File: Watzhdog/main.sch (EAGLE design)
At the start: 44 parts, among them CN1 MICROUSB(MC-5F-02), IC1 C8051F381-GM, IC3 N25Q512A, IC6 MPU-9250, U1 MCP73831, U2 TPS61201

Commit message: 回路図修正完了 モジュールごとに見やすくした DCDC の高周波ラインを分離 各所パスコン追加 EEPROM のCS ラインにプルアップ追加
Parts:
- added C12, C14: 0.1u, reg,cap:C-1005
- added C13, C4: 22uF, CH_passive:CAP0805
- added R6: 100k, reg,cap:R-1005
- R26: value 1k -> 100k
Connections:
- net N$5 renamed PWR_EN_1
- net N$6 renamed PWR_EN
- net N$7 renamed PWR_EN_2
- removed net VBAT: C2.1, JP1.+, L1.2, R2.2, S1.1, S1.2, U1.VBAT, U2.VIN
- removed net VCC: C1.1, C10.P$2, C11.P$2, C6.1, C7.P$2, C9.P$2, IC1G$1.REGIN, IC1G$1.VDD, IC3G$1.!HOLD!/DQ3, IC3G$1.!WP!/VPP/DQ2, IC3G$1.VCC, IC6.RESV1, IC6.VDD, IC6.VDDIO, MP.TP, R11.P$2, U2.FB, U2.VOUT
- new net +3V3: C1.1, C10.P$2, C11.P$2, C13.1, C14.P$2, C6.1, C7.P$2, C9.P$2, IC1G$1.REGIN, IC1G$1.VDD, IC3G$1.!HOLD!/DQ3, IC3G$1.!WP!/VPP/DQ2, IC3G$1.VCC, IC6.RESV1, IC6.VDD, IC6.VDDIO, MP.TP, R11.P$2, R6.P$2, U2.FB, U2.VOUT
- new net PGND: C1.2, C12.P$1, C13.2, C4.2, U2.PAD@1, U2.PAD@2, U2.PAD@3, U2.PAD@4, U2.PAD@5, U2.PGND
- new net VDD_BATT: C12.P$2, C2.1, C4.1, JP1.+, L1.2, R2.2, S1.1, S1.2, U1.VBAT, U2.VIN
- net DGND: now also C14.P$1; no longer C1.2, U2.PAD@1, U2.PAD@2, U2.PAD@3, U2.PAD@4, U2.PAD@5, U2.PGND
- net EEPROM_!CS: now also R6.P$1
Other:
- moved on the sheet: C1, C10, C2, C3, C5, C6, CN1, D11, D2, D3, D4, FET1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

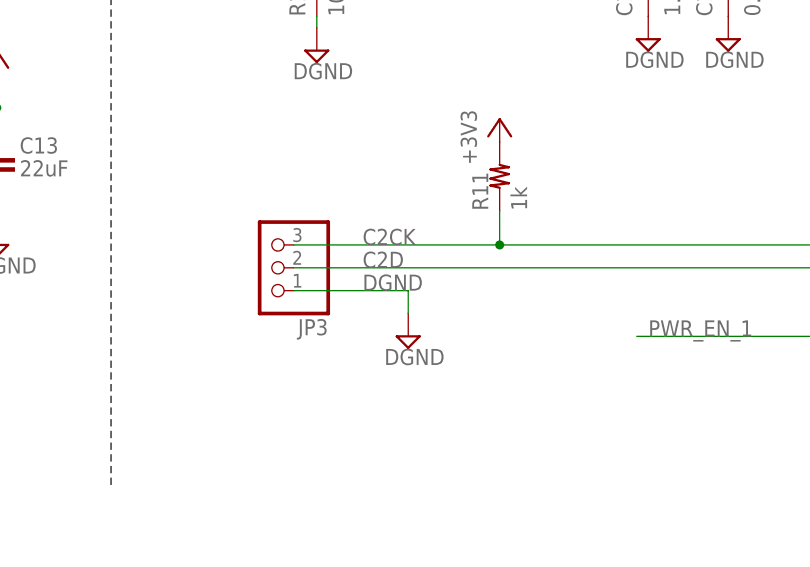
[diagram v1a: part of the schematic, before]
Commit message: 部品配置の再検討中 SW電源，充電IC，USB インターフェース周りは完了 残：モータFET，マイコン，周辺IC
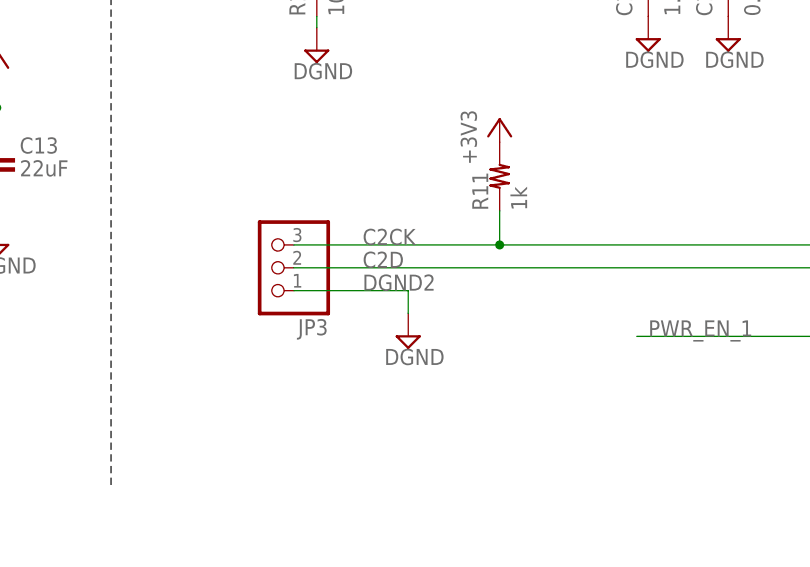
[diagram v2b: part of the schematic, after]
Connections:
- net DGND renamed DGND2
- net N$1 renamed VAUX
- net N$2 renamed LIN
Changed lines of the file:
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@@
 <setting verticaltext="up"/>
 </settings>
-<grid distance="0.05" unitdist="inch" unit="inch" style="lines" multiple="1" display="yes" altdistance="0.01" altunitdist="inch" altunit="inch"/>
+<grid distance="0.1" unitdist="inch" unit="inch" style="lines" multiple="1" display="no" altdistance="0.01" altunitdist="inch" altunit="inch"/>
 <layers>
 <layer number="1" name="Top" color="4" fill="1" visible="no" active="no"/>
@@
 </segment>
 </net>
-<net name="N$2" class="1">
+<net name="LIN" class="1">
 <segment>
 <wire x1="250.19" y1="30.48" x2="252.73" y2="30.48" width="0.1524" layer="91"/>
@@
 </segment>
 </net>
-<net name="N$1" class="0">
+<net name="VAUX" class="0">
 <segment>
 <wire x1="260.35" y1="22.86" x2="260.35" y2="25.4" width="0.1524" layer="91"/>
@@
 </segment>
 </net>
-<net name="DGND" class="1">
+<net name="DGND2" class="1">
 <segment>
 <pinref part="C7" gate="G$1" pin="P$1"/>

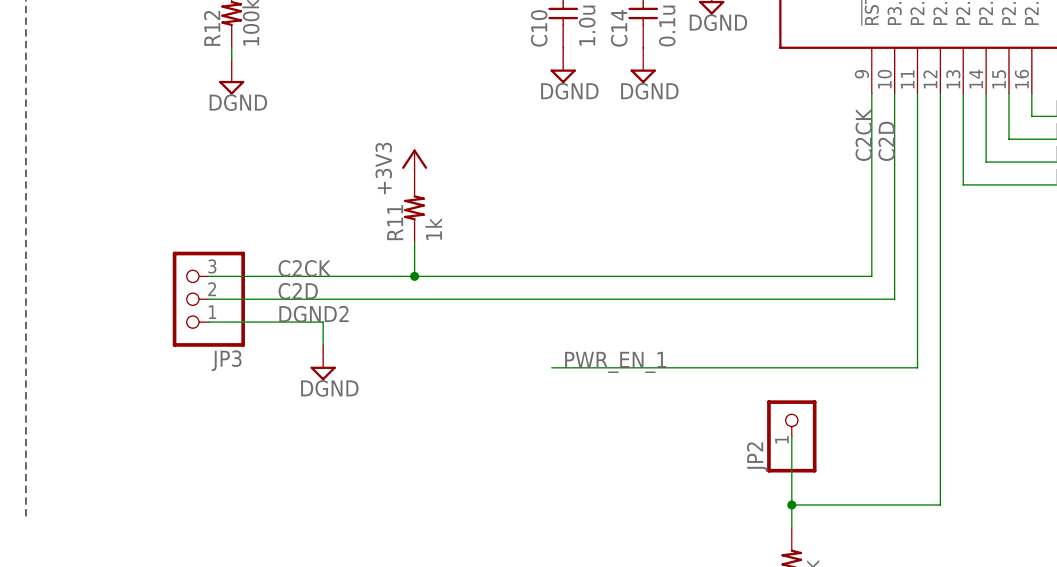
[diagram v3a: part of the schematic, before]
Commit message: GND 以外の配線概ね終了 PGNDとDGND を接合する準備を開始
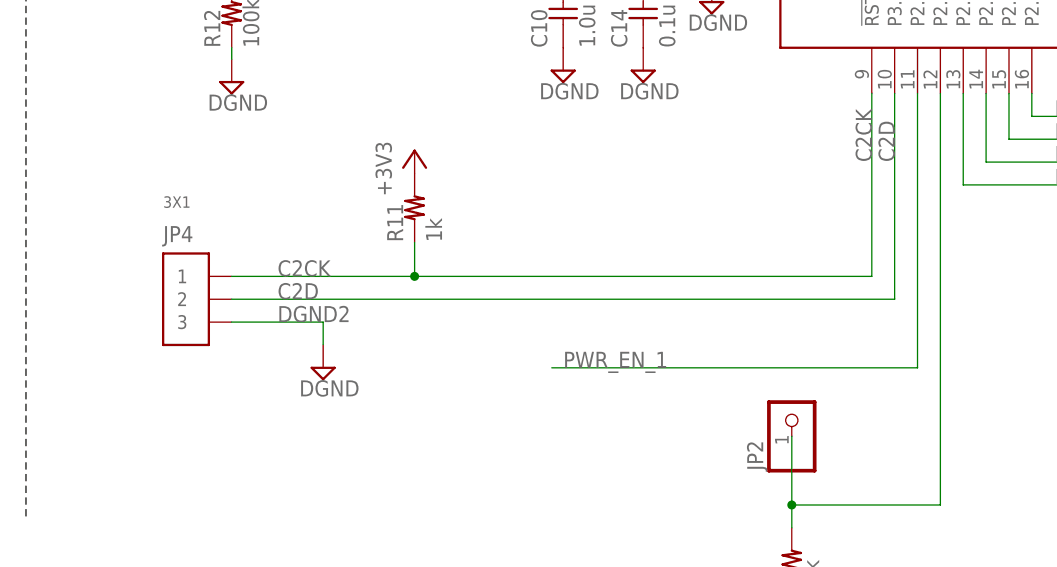
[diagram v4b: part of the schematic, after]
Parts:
- removed JP3: (no value), pinhead:PINHD-1X3
- added JP4: 3X1, pin_header:3X1
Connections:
- net C2CK: now also JP4.1; no longer JP3.3
- net C2D: now also JP4.2; no longer JP3.2
- net DGND2: now also JP4.3; no longer JP3.1
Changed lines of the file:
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@@
 <part name="R17" library="reg,cap" deviceset="R-" device="1005" value="100"/>
 <part name="JP2" library="pinhead" library_urn="urn:adsk.eagle:library:325" deviceset="PINHD-1X1" device="" package3d_urn="urn:adsk.eagle:package:22485/2"/>
-<part name="JP3" library="pinhead" library_urn="urn:adsk.eagle:library:325" deviceset="PINHD-1X3" device="" package3d_urn="urn:adsk.eagle:package:22458/2"/>
 <part name="CN1" library="Connector" deviceset="MICROUSB(MC-5F-02)" device=""/>
 <part name="C2" library="CH_passive" deviceset="CAP" device="0805" value="22uF"/>
@@
 <part name="R6" library="reg,cap" deviceset="R-" device="1005" value="100k"/>
 <part name="+3V7" library="supply1" deviceset="+3V3" device=""/>
+<part name="JP4" library="pin_header" deviceset="3X1" device=""/>
 </parts>
 <sheets>
@@
 <instance part="R17" gate="G$1" x="339.09" y="81.28"/>
 <instance part="JP2" gate="G$1" x="379.73" y="-2.54" rot="R90"/>
-<instance part="JP3" gate="A" x="312.42" y="10.16" rot="R180"/>
 <instance part="CN1" gate="G$1" x="26.67" y="49.53" smashed="yes">
 <attribute name="NAME" x="20.32" y="42.037" size="1.778" layer="95"/>
@@
 <instance part="R6" gate="G$1" x="401.32" y="157.48" rot="R90"/>
 <instance part="+3V7" gate="G$1" x="401.32" y="165.1"/>
+<instance part="JP4" gate="G$1" x="314.96" y="10.16"/>
 </instances>
 <busses>
@@
 </segment>
 <segment>
-<pinref part="JP3" gate="A" pin="1"/>
-<wire x1="314.96" y1="7.62" x2="327.66" y2="7.62" width="0.1524" layer="91"/>
+<wire x1="317.5" y1="7.62" x2="327.66" y2="7.62" width="0.1524" layer="91"/>
 <wire x1="327.66" y1="7.62" x2="327.66" y2="5.08" width="0.1524" layer="91"/>
 <pinref part="SUPPLY1" gate="G$1" pin="DGND"/>
 <label x="322.58" y="7.62" size="1.778" layer="95"/>
+<pinref part="JP4" gate="G$1" pin="3"/>
 </segment>
 <segment>
@@
 <pinref part="IC1" gate="G$1" pin="!RST!/C2CK"/>
 <pinref part="R11" gate="G$1" pin="P$1"/>
-<pinref part="JP3" gate="A" pin="3"/>
-<wire x1="337.82" y1="12.7" x2="314.96" y2="12.7" width="0.1524" layer="91"/>
+<wire x1="337.82" y1="12.7" x2="317.5" y2="12.7" width="0.1524" layer="91"/>
+<pinref part="JP4" gate="G$1" pin="1"/>
 </segment>
 </net>
 <net name="C2D" class="0">
 <segment>
-<wire x1="314.96" y1="10.16" x2="391.16" y2="10.16" width="0.1524" layer="91"/>
+<wire x1="317.5" y1="10.16" x2="391.16" y2="10.16" width="0.1524" layer="91"/>
 <wire x1="391.16" y1="33.02" x2="391.16" y2="10.16" width="0.1524" layer="91"/>
 <label x="391.16" y="25.4" size="1.778" layer="95" rot="R90"/>
 <label x="322.58" y="10.16" size="1.778" layer="95"/>
 <pinref part="IC1" gate="G$1" pin="P3.0/C2D"/>
-<pinref part="JP3" gate="A" pin="2"/>
-</segment>
-</net>
+<pinref part="JP4" gate="G$1" pin="2"/>
+</segment>
+</net>

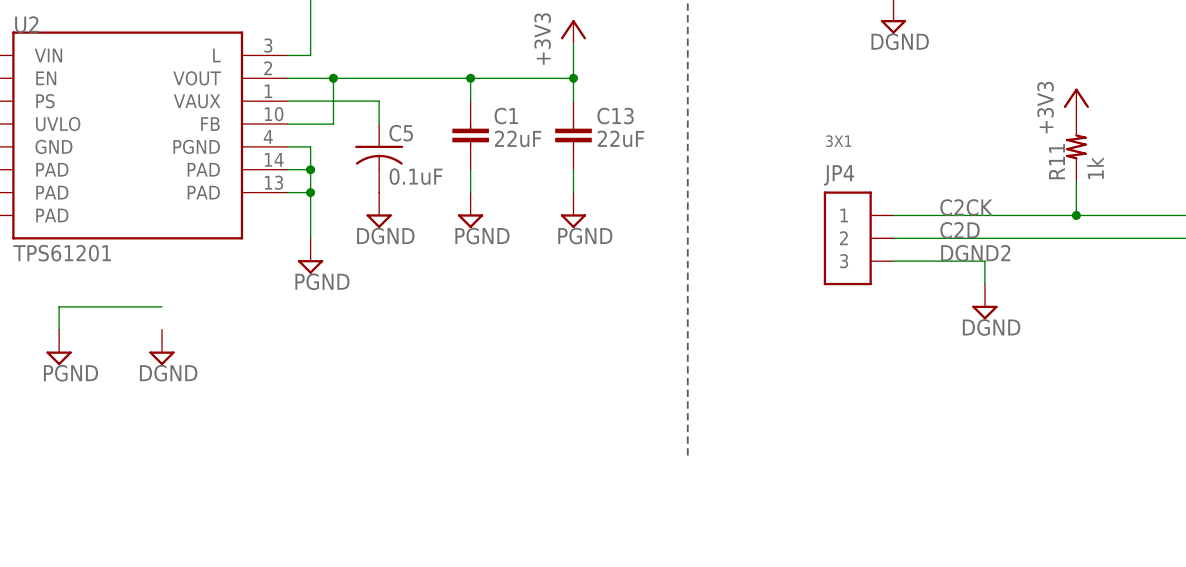
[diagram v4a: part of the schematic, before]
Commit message: airwire 0 本 GND 含めポリゴン貼り完了
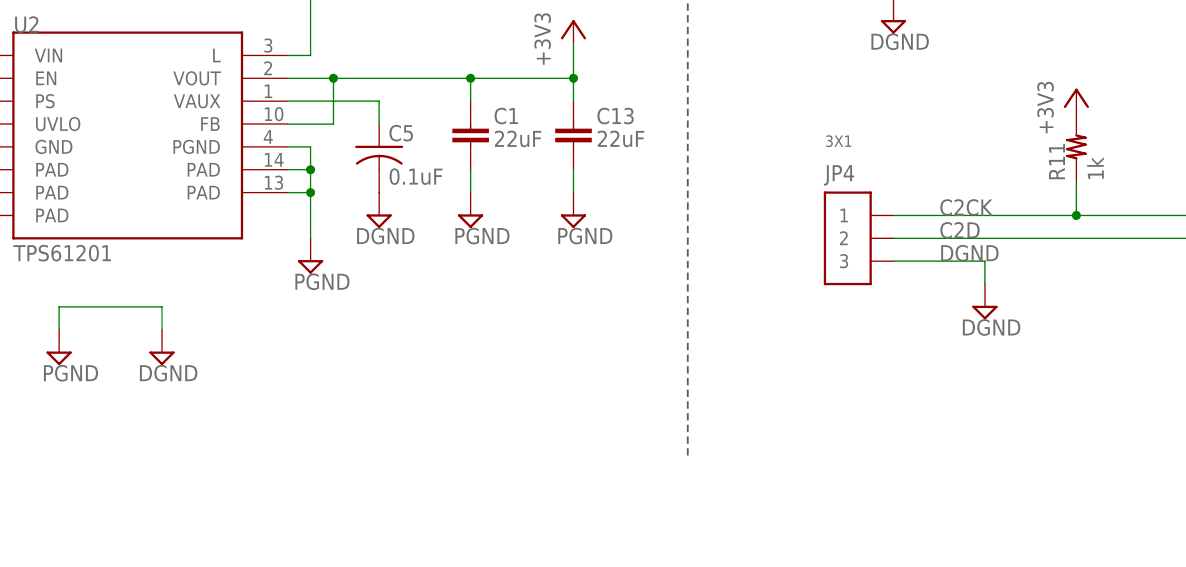
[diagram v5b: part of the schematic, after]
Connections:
- removed net DGND2: C10.P$1, C11.P$1, C14.P$1, C2.2, C3.2, C5.2, C6.2, C7.P$1, C8.P$1, C9.P$1, CN1.P$5, D3.1, FET1.S, IC1G$1.GND, IC1G$2.BOTTOM/GND, IC3G$1.VSS, IC3G$2.BOTTOM/GND, IC6.FSSYNC, IC6.GND, IC6.RESV20, JP1.-, JP4.3, LED1.K, R12.P$1, R13.P$1, R14.P$1, R15.P$1, R26.P$1, R4.2, R5.1, U1.VSS, U2.GND, U2.PS
- removed net PGND: C1.2, C12.P$1, C13.2, C4.2, U2.PAD@1, U2.PAD@2, U2.PAD@3, U2.PAD@4, U2.PAD@5, U2.PGND
- new net DGND: C1.2, C10.P$1, C11.P$1, C12.P$1, C13.2, C14.P$1, C2.2, C3.2, C4.2, C5.2, C6.2, C7.P$1, C8.P$1, C9.P$1, CN1.P$5, D3.1, FET1.S, IC1G$1.GND, IC1G$2.BOTTOM/GND, IC3G$1.VSS, IC3G$2.BOTTOM/GND, IC6.FSSYNC, IC6.GND, IC6.RESV20, JP1.-, JP4.3, LED1.K, R12.P$1, R13.P$1, R14.P$1, R15.P$1, R26.P$1, R4.2, R5.1, U1.VSS, U2.GND, U2.PAD@1, U2.PAD@2, U2.PAD@3, U2.PAD@4, U2.PAD@5, U2.PGND, U2.PS

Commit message: シルク調整完了 スペースがないため，すべてを表示できないため，ガーバー出力はしない方が良さそう
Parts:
- removed D11: RED, SparkFun-LED:LED-RED0603
- removed IC6: MPU-9250, GYRO:MPU-9250
- removed JP4: 3X1, pin_header:3X1
- removed R17: 100, reg,cap:R-1005
- removed R26: 100k, reg,cap:R-1005
- added D1: SP0503BAH, diode:SP0503BAH
- added IC2: C8051F381-GM, C8051F34x:C8051F381-GM
- added J1: JST, SparkFun-Connectors:JST_2MM_MALE
- added R7: 10k, reg,cap:R-1005
- added R8: 1k (Optional), reg,cap:R-1005
- C1: value 22uF -> 4.7uF; device CH_passive:CAP0805 -> SparkFun-Capacitors:4.7UF-6.3V-10%(0603)0603
- C10: value 1.0u -> 0.1u
- C12: value 0.1u -> 10n
- C13, C4: value 22uF -> 0.1u; device CH_passive:CAP0805 -> reg,cap:C-1005
- C3: value 4.7uF -> 22uF; device SparkFun-Capacitors:4.7UF-6.3V-10%(0603)0603 -> CH_passive:CAP0805
- C7: value 10n -> 22uF; device reg,cap:C-1005 -> CH_passive:CAP0805
- C8: value 0.1u -> 22uF; device reg,cap:C-1005 -> CH_passive:CAP0805
- C9: value 0.1u -> 1.0u
- D2: value CUS08F30 -> RED; device diode:DIODE-SOD323-W -> SparkFun-LED:LED-RED0603
- D3: value SP0503BAH -> CUS08F30; device diode:SP0503BAH -> diode:DIODE-SOD323-W
- IC1: value C8051F381-GM -> N25Q512A; device C8051F34x:C8051F381-GM -> EEPROM:N25Q512A
- IC3: value N25Q512A -> MPU-9250; device EEPROM:N25Q512A -> GYRO:MPU-9250
- JP1: value JST -> 3X1; device SparkFun-Connectors:JST_2MM_MALE -> pin_header:3X1
- R1: value 1k (Optional) -> 330; device reg,cap:R-1005 -> rcl:R-US_R0402
- R12: value 100k -> 100
- R15, R16, R9: value 10k -> 100k
- R2: value 2M -> 9.09k
- R3: value 330 -> 2M
- R4: value 9.09k -> 220k
- R5: value 220k -> 10k; device rcl:R-US_R0402 -> reg,cap:R-1005
- R6: value 100k -> 10k
- renumbered MN to TP2, MP to TP1
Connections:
- net +3V3: now also C12.P$2, C7.1, C8.1, IC1G$1.!HOLD!/DQ3, IC1G$1.!WP!/VPP/DQ2, IC1G$1.VCC, IC2G$1.REGIN, IC2G$1.VDD, IC3.RESV1, IC3.VDD, IC3.VDDIO, R16.P$2; no longer C1.1, C13.1, C7.P$2, IC1G$1.REGIN, IC1G$1.VDD, IC3G$1.!HOLD!/DQ3, IC3G$1.!WP!/VPP/DQ2, IC3G$1.VCC, IC6.RESV1, IC6.VDD, IC6.VDDIO, R6.P$2
- net C2CK: now also IC2G$1.!RST!/C2CK, JP1.1; no longer IC1G$1.!RST!/C2CK, JP4.1
- net C2D: now also IC2G$1.P3.0/C2D, JP1.2; no longer IC1G$1.P3.0/C2D, JP4.2
- net D+: now also D1.2, IC2G$1.D+; no longer D3.2, IC1G$1.D+
- net D-: now also D1.3, IC2G$1.D-; no longer D3.3, IC1G$1.D-
- net DGND: now also C13.P$1, C4.P$1, C7.2, C8.2, D1.1, IC1G$1.VSS, IC2G$1.GND, IC2G$2.BOTTOM/GND, IC3.FSSYNC, IC3.GND, IC3.RESV20, J1.-, JP1.3, R2.2, R4.1, R6.P$1, R7.P$1, R9.P$1; no longer C13.2, C4.2, C7.P$1, C8.P$1, D3.1, IC1G$1.GND, IC3G$1.VSS, IC3G$2.BOTTOM/GND, IC6.FSSYNC, IC6.GND, IC6.RESV20, JP1.-, JP4.3, R12.P$1, R14.P$1, R26.P$1, R4.2, R5.1
- net EEPROM_!CS: now also IC1G$1.!CS, IC2G$1.P0.7, R16.P$1; no longer IC1G$1.P0.7, IC3G$1.!CS, R6.P$1
- net EEPROM_MISO: now also IC1G$1.DQ1, IC2G$1.P0.6; no longer IC1G$1.P0.6, IC3G$1.DQ1
- net EEPROM_MOSI: now also IC1G$1.DQ0, IC2G$1.P0.5; no longer IC1G$1.P0.5, IC3G$1.DQ0
- net EEPROM_SCK: now also IC1G$1.CLK, IC2G$1.P0.4, R15.P$2; no longer IC1G$1.P0.4, IC3G$1.CLK, R26.P$2
- net IMU_!CS: now also IC2G$1.P2.2, IC3.NCS; no longer IC1G$1.P2.2, IC6.NCS
- net IMU_MISO: now also IC2G$1.P2.5, IC3.AD0/SDO; no longer IC1G$1.P2.5, IC6.AD0/SDO
- net IMU_MOSI: now also IC2G$1.P2.4, IC3.SDA/SDI; no longer IC1G$1.P2.4, IC6.SDA/SDI
- net IMU_SCK: now also IC2G$1.P2.3, IC3.SCL/SCLK; no longer IC1G$1.P2.3, IC6.SCL/SCLK
- net N$11: now also D3.A, R5.P$2, R7.P$2; no longer D2.A, R13.P$2, R16.P$2
- net N$13: now also C13.P$2, IC3.REGOUT; no longer C8.P$2, IC6.REGOUT
- net N$15: now also IC2G$1.P2.6, R14.P$2; no longer IC1G$1.P2.6, R9.P$2
- net N$18: now also IC2G$1.VBUS; no longer IC1G$1.VBUS
- net N$3: now also D2.A, R1.1; no longer D11.A, R3.1
- net N$8: now also R12.P$1; no longer R17.P$1
- net N$9: now also R14.P$1; no longer R9.P$1
- net PROG: now also R2.1; no longer R4.1
- net PWM: now also IC2G$1.P0.2/XTAL1, R12.P$2, R13.P$2; no longer IC1G$1.P0.2/XTAL1, R15.P$2, R17.P$2
- net PWR_EN: now also D3.C, R6.P$2; no longer D2.C, R14.P$2
- net PWR_EN_1: now also IC2G$1.P2.7, R5.P$1; no longer IC1G$1.P2.7, R16.P$1
- net PWR_EN_2: now also IC2G$1.P2.1, R8.P$1; no longer IC1G$1.P2.1, R1.P$1
- net STAT: now also D2.C; no longer D11.C
- net UVLO: now also R3.1, R4.2; no longer R2.1, R5.2
- net VBUS: now also C1.1, D1.4, R1.2, R8.P$2, R9.P$2; no longer C3.1, D3.4, R1.P$2, R12.P$2, R3.2
- net VDD_BATT: now also C3.1, C4.P$2, J1.+, R3.2; no longer C12.P$2, C4.1, JP1.+, R2.2
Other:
- moved on the sheet: C1, C10, C12, C14, C3, C6, C9, R12, R13, R14, R15, R16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
